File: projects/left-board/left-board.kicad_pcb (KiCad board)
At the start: 2 copper layers, 34.1 x 75.7 mm, 6 parts, among them J1 5051101292, SW1 TS06-667-25-BK-160-G-SMT-TR, SW2 TS06-667-25-BK-160-G-SMT-TR, SW3 TS06-667-25-BK-160-G-SMT-TR, SW4 TS06-667-25-BK-160-G-SMT-TR, SW5 TS06-667-25-BK-160-G-SMT-TR

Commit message: Fix wrong net name on left audio
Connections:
- net /LEFT_MOTOR.N renamed /LEFT_MOTOR_N
- net /LEFT_MOTOR.P renamed /LEFT_MOTOR_P
- net /LEFT_SPEAKER.N renamed /LEFT_SPEAKER_N
- net /LEFT_SPEAKER.P renamed /LEFT_SPEAKER_P
- J1 pad 2: /BUTTONS.B0 -> /BUTTONS_B0
- J1 pad 3: /BUTTONS.B1 -> /BUTTONS_B1
- J1 pad 4: /BUTTONS.B2 -> /BUTTONS_B2
- J1 pad 5: /BUTTONS.B3 -> /BUTTONS_B3
- J1 pad 6: /BUTTONS.B4 -> /BUTTONS_B4
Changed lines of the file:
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@@
 	)
 	(net 0 "")
-	(net 1 "/BUTTONS.B1")
-	(net 2 "/LEFT_MOTOR.P")
-	(net 3 "/BUTTONS.B2")
+	(net 1 "/LEFT_MOTOR_P")
+	(net 2 "/LEFT_SPEAKER_N")
+	(net 3 "/LEFT_SPEAKER_P")
 	(net 4 "GND")
-	(net 5 "/LEFT_SPEAKER.N")
-	(net 6 "/BUTTONS.B0")
-	(net 7 "3V3")
-	(net 8 "/BUTTONS.B4")
-	(net 9 "/LEFT_SPEAKER.P")
-	(net 10 "/BUTTONS.B3")
-	(net 11 "/LEFT_MOTOR.N")
-	(net 12 "/BUTTONS_B0")
-	(net 13 "/BUTTONS_B1")
-	(net 14 "/BUTTONS_B2")
-	(net 15 "/BUTTONS_B3")
-	(net 16 "/BUTTONS_B4")
+	(net 5 "/LEFT_MOTOR_N")
+	(net 6 "3V3")
+	(net 7 "/BUTTONS_B0")
+	(net 8 "/BUTTONS_B1")
+	(net 9 "/BUTTONS_B2")
+	(net 10 "/BUTTONS_B3")
+	(net 11 "/BUTTONS_B4")
 	(footprint "footprint-library:5051101292"
 		(layer "F.Cu")
@@
 			(size 0.3 1)
 			(layers "F.Cu" "F.Mask" "F.Paste")
-			(net 7 "3V3")
+			(net 6 "3V3")
 			(pinfunction "Pin_1")
 			(pintype "passive")
@@
 			(size 0.3 1)
 			(layers "F.Cu" "F.Mask" "F.Paste")
-			(net 6 "/BUTTONS.B0")
+			(net 7 "/BUTTONS_B0")
 			(pinfunction "Pin_2")
 			(pintype "passive")
@@
 			(size 0.3 1)
 			(layers "F.Cu" "F.Mask" "F.Paste")
-			(net 1 "/BUTTONS.B1")
+			(net 8 "/BUTTONS_B1")
 			(pinfunction "Pin_3")
 			(pintype "passive")
@@
 			(size 0.3 1)
 			(layers "F.Cu" "F.Mask" "F.Paste")
-			(net 3 "/BUTTONS.B2")
+			(net 9 "/BUTTONS_B2")
 			(pinfunction "Pin_4")
 			(pintype "passive")
@@
 			(size 0.3 1)
 			(layers "F.Cu" "F.Mask" "F.Paste")
-			(net 10 "/BUTTONS.B3")
+			(net 10 "/BUTTONS_B3")
 			(pinfunction "Pin_5")
 			(pintype "passive")
@@
 			(size 0.3 1)
 			(layers "F.Cu" "F.Mask" "F.Paste")
-			(net 8 "/BUTTONS.B4")
+			(net 11 "/BUTTONS_B4")
 			(pinfunction "Pin_6")
 			(pintype "passive")
@@
 			(size 0.3 1)
 			(layers "F.Cu" "F.Mask" "F.Paste")
-			(net 9 "/LEFT_SPEAKER.P")
+			(net 3 "/LEFT_SPEAKER_P")
 			(pinfunction "Pin_8")
 			(pintype "passive")
@@
 			(size 0.3 1)
 			(layers "F.Cu" "F.Mask" "F.Paste")
-			(net 5 "/LEFT_SPEAKER.N")
+			(net 2 "/LEFT_SPEAKER_N")
 			(pinfunction "Pin_9")
 			(pintype "passive")
@@
 			(size 0.3 1)
 			(layers "F.Cu" "F.Mask" "F.Paste")
-			(net 2 "/LEFT_MOTOR.P")
+			(net 1 "/LEFT_MOTOR_P")
 			(pinfunction "Pin_11")
 			(pintype "passive")
@@
 			(size 0.3 1)
 			(layers "F.Cu" "F.Mask" "F.Paste")
-			(net 11 "/LEFT_MOTOR.N")
+			(net 5 "/LEFT_MOTOR_N")
 			(pinfunction "Pin_12")
 			(pintype "passive")
@@
 			(size 1.6 1.4)
 			(layers "B.Cu" "B.Mask" "B.Paste")
-			(net 16 "/BUTTONS_B4")
+			(net 11 "/BUTTONS_B4")
 			(pintype "passive")
 			(solder_mask_margin 0.102)
@@
 			(size 1.6 1.4)
 			(layers "B.Cu" "B.Mask" "B.Paste")
-			(net 16 "/BUTTONS_B4")
+			(net 11 "/BUTTONS_B4")
 			(pintype "passive")
 			(solder_mask_margin 0.102)
@@
 			(size 1.6 1.4)
 			(layers "B.Cu" "B.Mask" "B.Paste")
-			(net 15 "/BUTTONS_B3")
+			(net 10 "/BUTTONS_B3")
 			(pintype "passive")
 			(solder_mask_margin 0.102)
@@
 			(size 1.6 1.4)
 			(layers "B.Cu" "B.Mask" "B.Paste")
-			(net 15 "/BUTTONS_B3")
+			(net 10 "/BUTTONS_B3")
 			(pintype "passive")
 			(solder_mask_margin 0.102)
@@
 			(size 1.6 1.4)
 			(layers "B.Cu" "B.Mask" "B.Paste")
-			(net 13 "/BUTTONS_B1")
+			(net 8 "/BUTTONS_B1")
 			(pintype "passive")
 			(solder_mask_margin 0.102)
@@
 			(size 1.6 1.4)
 			(layers "B.Cu" "B.Mask" "B.Paste")
-			(net 13 "/BUTTONS_B1")
+			(net 8 "/BUTTONS_B1")
 			(pintype "passive")
 			(solder_mask_margin 0.102)
@@
 			(size 1.6 1.4)
 			(layers "B.Cu" "B.Mask" "B.Paste")
-			(net 12 "/BUTTONS_B0")
+			(net 7 "/BUTTONS_B0")
 			(pintype "passive")
 			(solder_mask_margin 0.102)
@@
 			(size 1.6 1.4)
 			(layers "B.Cu" "B.Mask" "B.Paste")
-			(net 12 "/BUTTONS_B0")
+			(net 7 "/BUTTONS_B0")
 			(pintype "passive")
 			(solder_mask_margin 0.102)
@@
 			(size 1.6 1.4)
 			(layers "B.Cu" "B.Mask" "B.Paste")
-			(net 14 "/BUTTONS_B2")
+			(net 9 "/BUTTONS_B2")
 			(pintype "passive")
 			(solder_mask_margin 0.102)
@@
 			(size 1.6 1.4)
 			(layers "B.Cu" "B.Mask" "B.Paste")
-			(net 14 "/BUTTONS_B2")
-			(pintype "passive")
-			(solder_mask_margin 0.102)
+			(net 9 "/BUTTONS_B2")
+			(pintype "passive")
+			(solder_mask_margin 0.102)

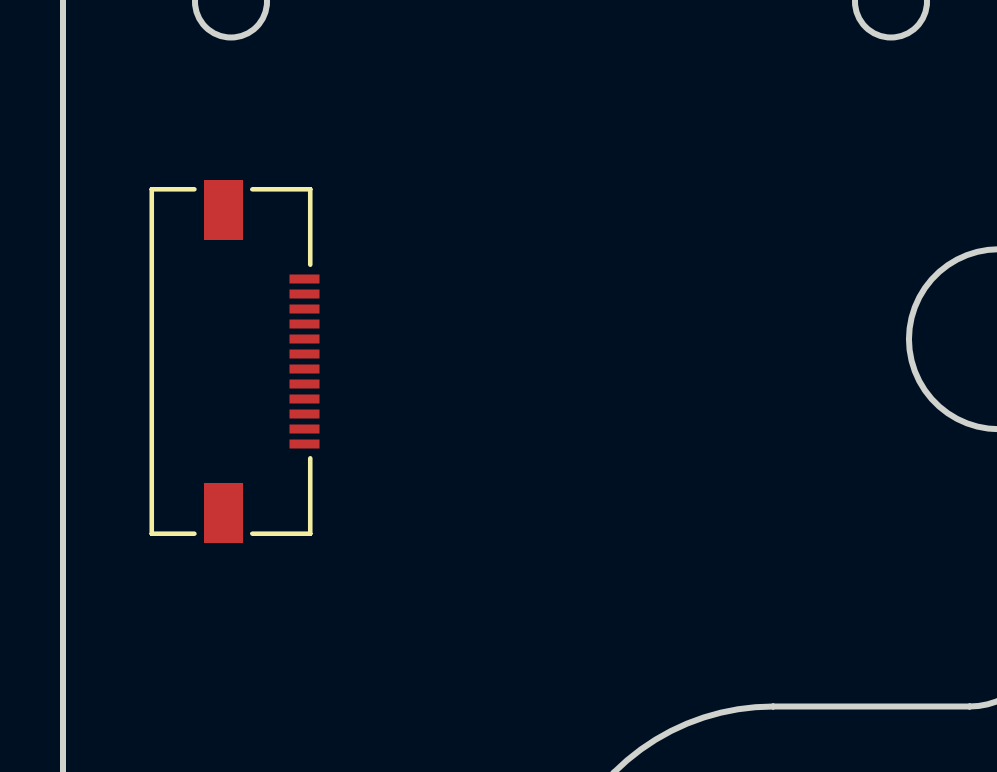
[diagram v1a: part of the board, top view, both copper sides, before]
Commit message: Position board-to-board connectors
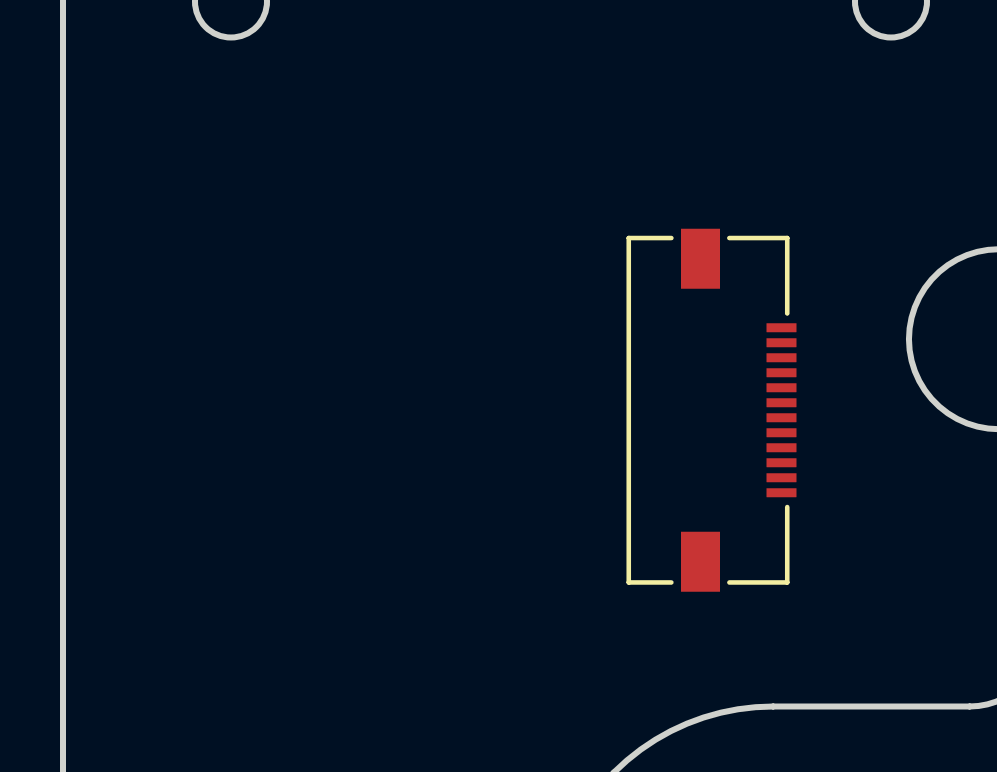
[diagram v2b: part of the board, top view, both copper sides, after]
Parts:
- moved J1 16.0 mm to (169.1, 121.5)
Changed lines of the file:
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@@
 	(footprint "footprint-library:5051101292"
 		(layer "F.Cu")
-		(at 153.149999 119.86973 -90)
+		(at 169.05 121.494715 -90)
 		(property "Reference" "J1"
 			(at -0.1016 -6.35 90)
@@
 		(layer "User.1")
 	)
+	(gr_line
+		(start 153.149999 109.06973)
+		(end 153.149999 133.9197)
+		(stroke
+			(width 0.05)
+			(type default)
+		)
+		(layer "User.1")
+	)
+	(gr_line
+		(start 147.55 98.928077)
+		(end 181.649999 98.928077)
+		(stroke
+			(width 0.05)
+			(type default)
+		)
+		(layer "User.1")
+	)
+	(gr_line
+		(start 147.55 121.494715)
+		(end 162.05 121.494715)
+		(stroke
+			(width 0.05)
+			(type default)
+		)
+		(layer "User.1")
+	)
